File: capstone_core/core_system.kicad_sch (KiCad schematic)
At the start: 0 parts

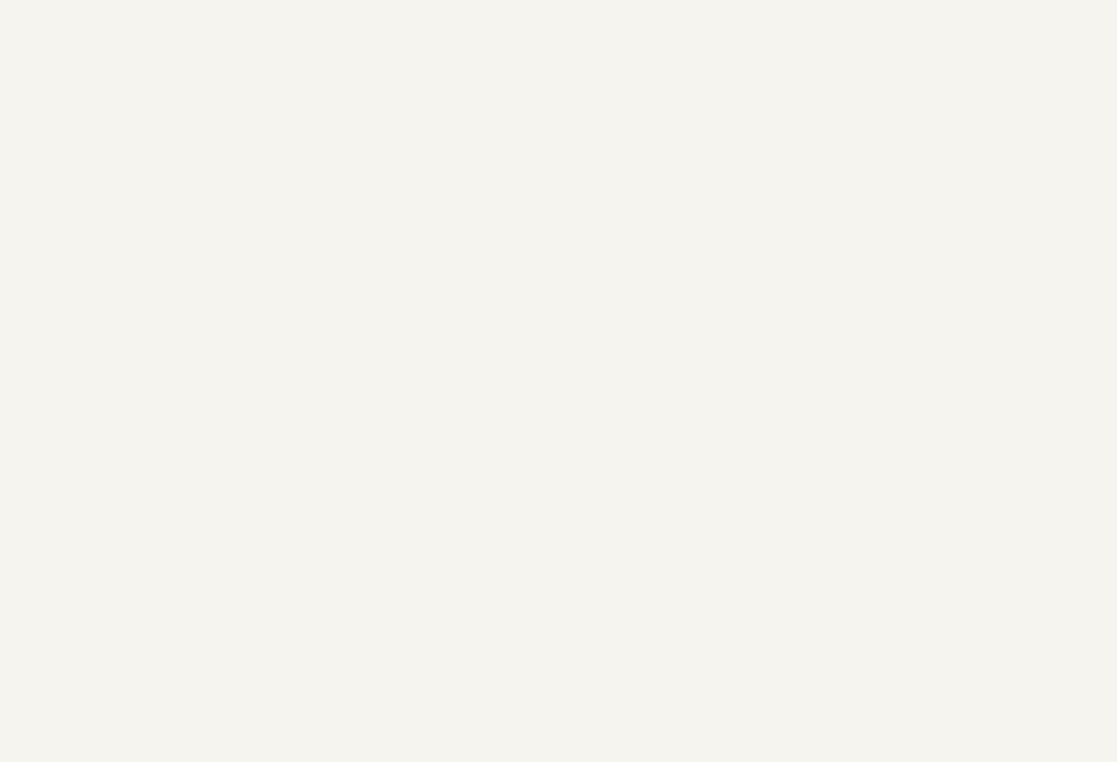
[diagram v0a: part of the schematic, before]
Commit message: adding connectors, components, and footprints
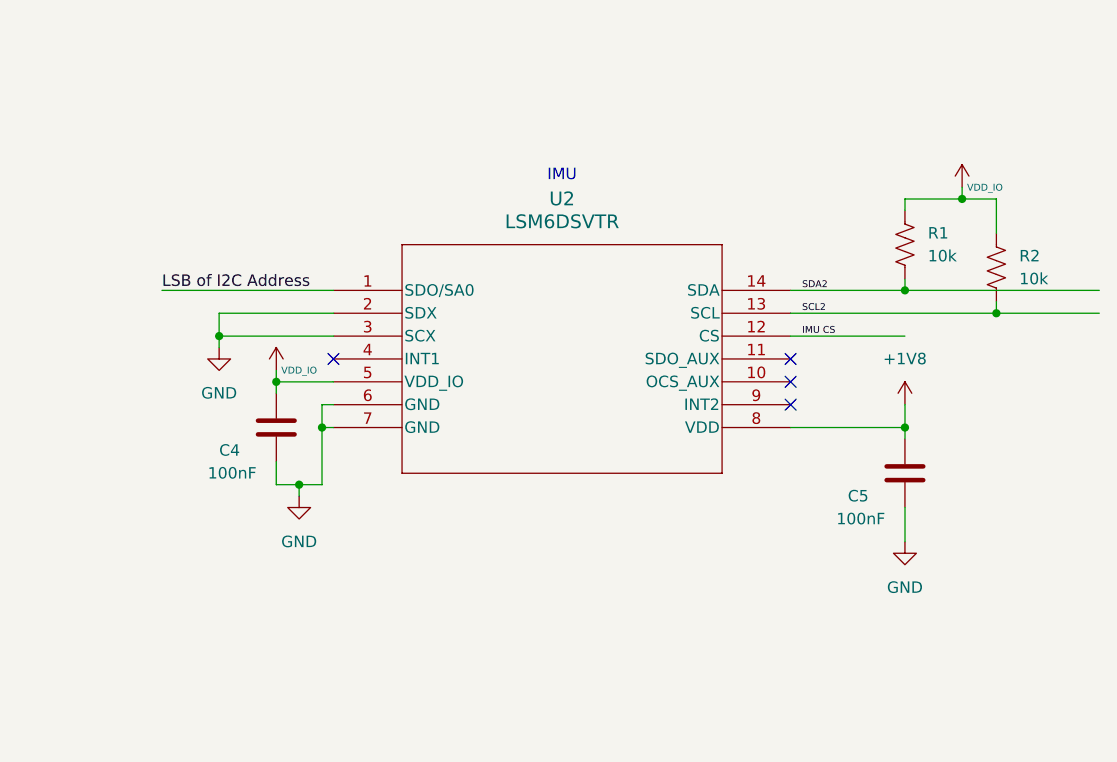
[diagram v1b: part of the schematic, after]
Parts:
- added C4, C5: 100nF, symbol Device:C
- added R1, R2: 10k, symbol Device:R_US
- added U2: LSM6DSVTR, Capstone Footprints:IMU_LGA14-L_2P59X3P1X0P5_STM-M, symbol Capstone Symbols:LSM6DSVTR
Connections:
- new net +1V8: C5.1, U2.8 (VDD)
- new net GND: C4.2, C5.2, U2.2 (SDX), U2.3 (SCX), U2.6 (GND), U2.7 (GND)
- new net IMU CS: U2.12 (CS)
- new net LSB of I2C Address: U2.1 (SDO/SA0)
- new net SCL2: R2.2, U2.13 (SCL)
- new net SDA2: R1.2, U2.14 (SDA)
- new net VDD_IO: C4.1, R1.1, R2.1, U2.5 (VDD_IO)
- no-connect marks 0 -> 4
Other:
- note added: "IMU"

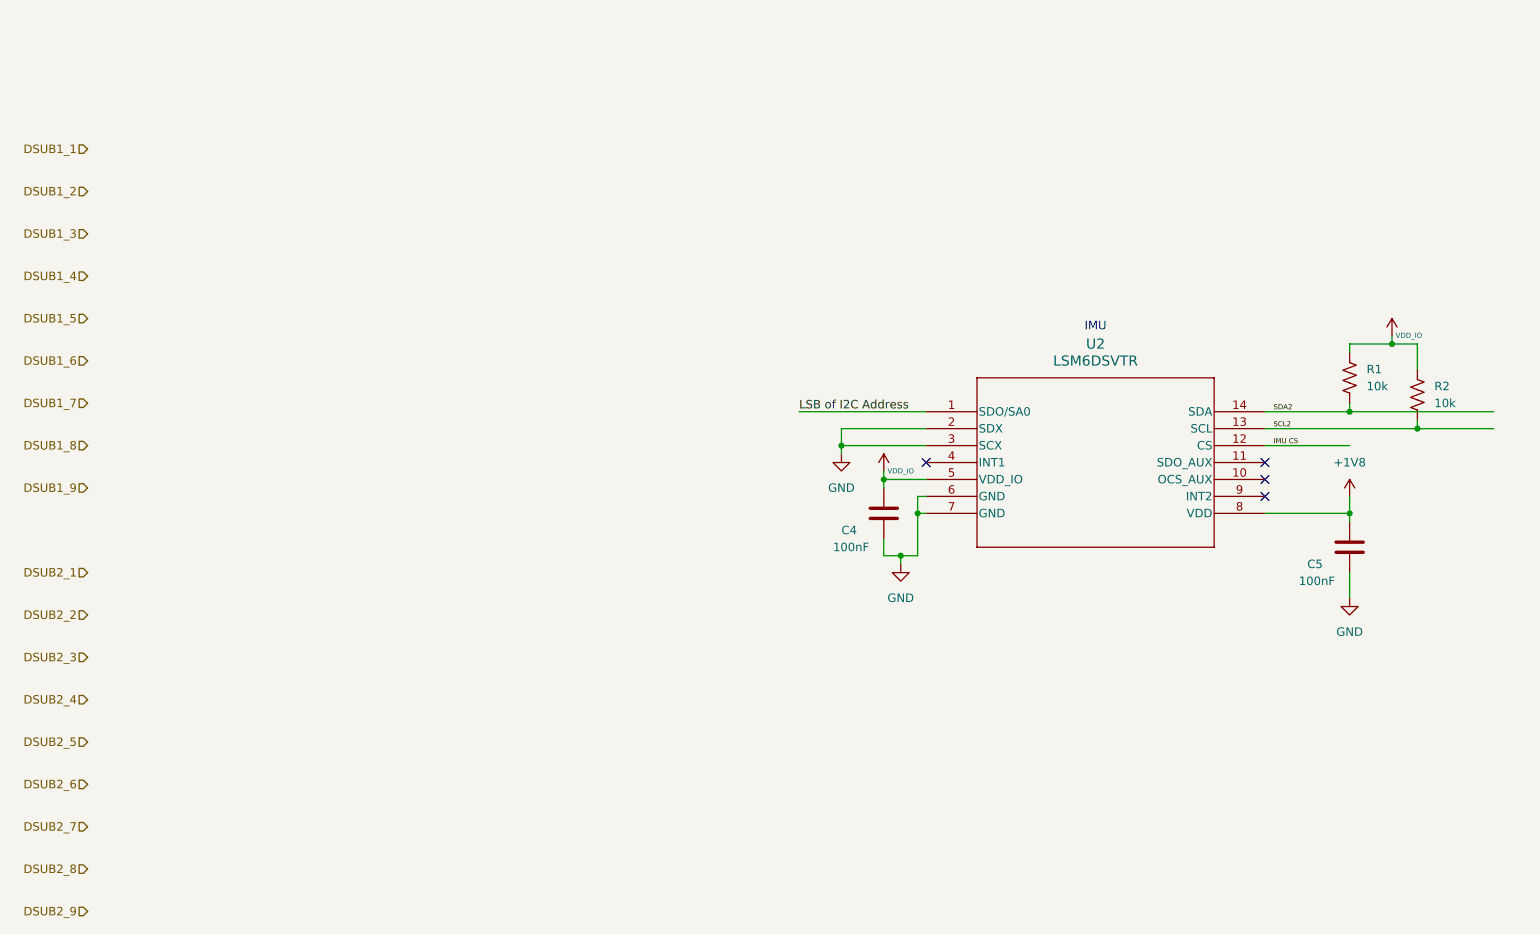
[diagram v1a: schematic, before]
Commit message: Add ZED-F9P & level shifter
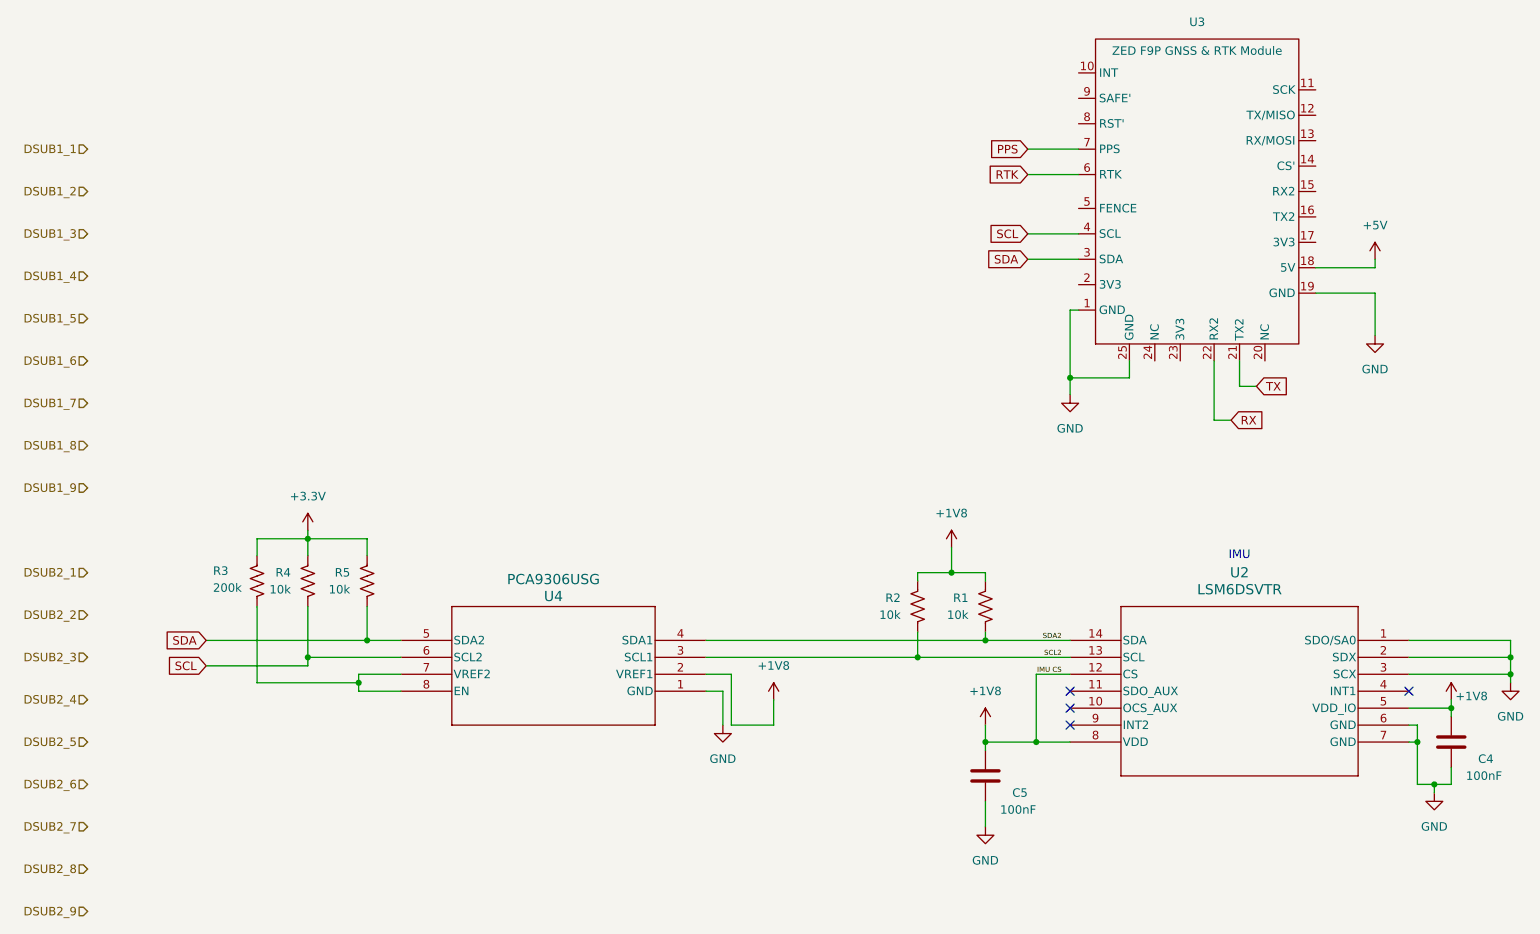
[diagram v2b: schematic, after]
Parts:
- added R3: 200k, symbol Device:R_US
- added R4, R5: 10k, symbol Device:R_US
- added U3: ZED F9P GNSS & RTK Module, ZED-F9P:Zed F9P, symbol ZED_F9P:ZED-F9P
- added U4: PCA9306USG, US8_2P40X2P10_ONS, symbol NLA9306USG:PCA9306USG
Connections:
- net IMU CS is gone; now on net +1V8: U2.12 (CS)
- net LSB of I2C Address is gone; now on net GND: U2.1 (SDO/SA0)
- net VDD_IO is gone; now on net +1V8: C4.1, R1.1, R2.1, U2.5 (VDD_IO)
- net +1V8: now also U4.2 (VREF1)
- net GND: now also U3.1 (GND), U3.19 (GND), U3.25 (GND), U4.1 (GND)
- net SCL2: now also U4.3 (SCL1)
- net SDA2: now also U4.4 (SDA1)
- new net: R3.2, U4.7 (VREF2), U4.8 (EN)
- new net +3.3V: R3.1, R4.1, R5.1
- new net +5V: U3.18 (5V)
- new net PPS: U3.7 (PPS)
- new net RTK: U3.6 (RTK)
- new net RX: U3.22 (RX2)
- new net SCL: R4.2, U3.4 (SCL), U4.6 (SCL2)
- new net SDA: R5.2, U3.3 (SDA), U4.5 (SDA2)
- new net TX: U3.21 (TX2)
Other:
- moved on the sheet: C4, C5, R1, R2, U2
